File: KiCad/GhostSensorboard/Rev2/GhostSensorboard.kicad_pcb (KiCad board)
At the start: 2 copper layers, 50 x 50 mm, 43 parts, among them P1 StartModule, P2 SteeringServo, P3 Motor, P4 CONN_02X30, Q1 BSS138, Q2 BSS138, SW1 SW_Push, U1 TCA9548ARGER, U10 GP2Y0E02B, U11 GP2Y0E02B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

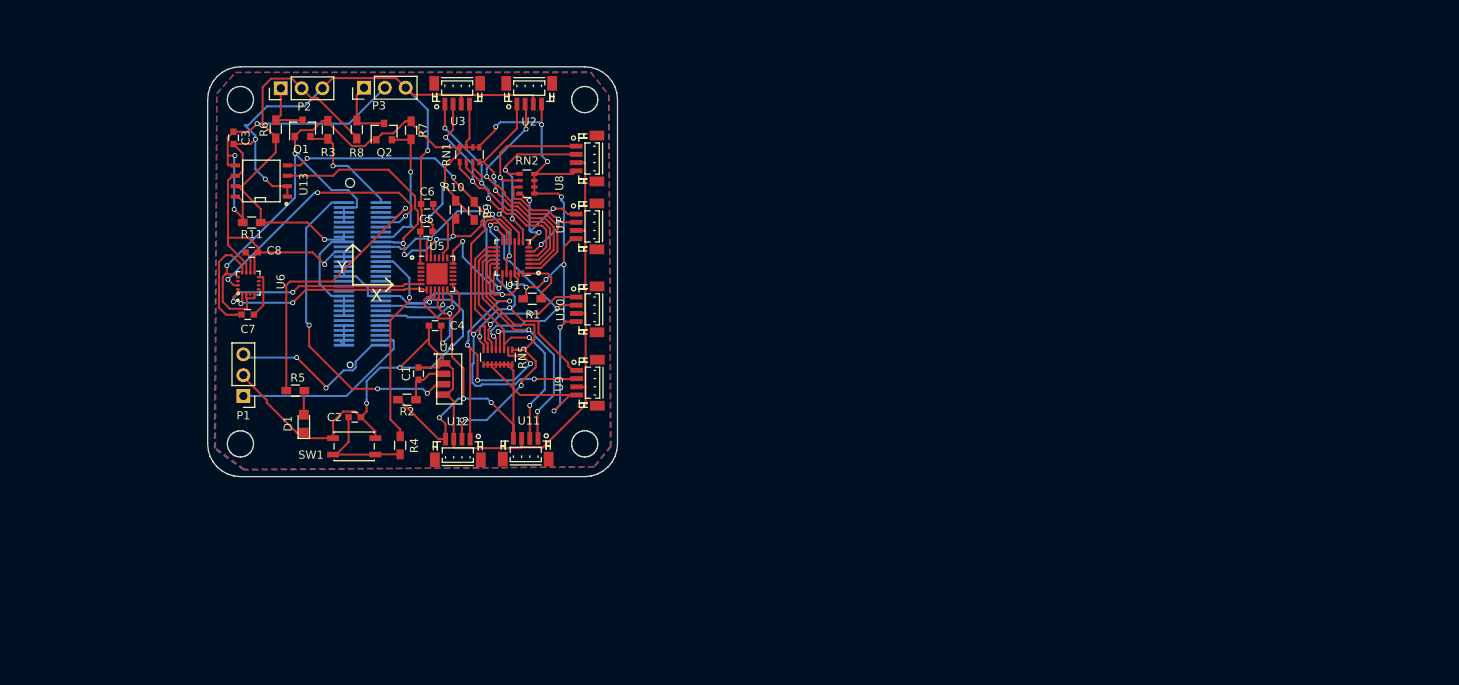
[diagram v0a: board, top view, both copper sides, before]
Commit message: Made a connectorboard
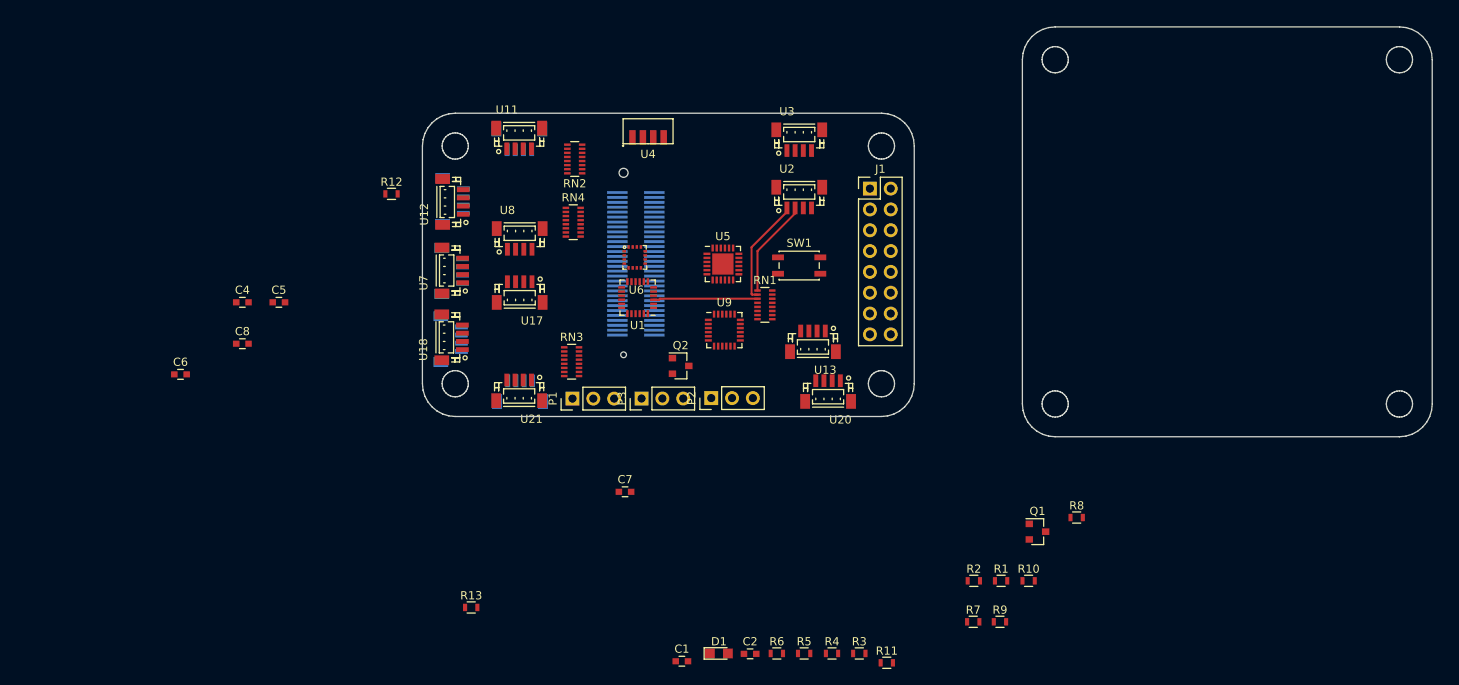
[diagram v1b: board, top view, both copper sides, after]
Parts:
- removed C3: 0.1-1uF, Capacitors_SMD:C_0603
- removed RN5: R_Pack08, Resistors_SMD:R_Array_Convex_8x0602
- added J1: CONN_02X08, Pin_Headers:Pin_Header_Straight_2x08_Pitch2.54mm, F.Cu at (171.5, 90.0)
- added R12: 2k2, Resistors_SMD:R_0603, F.Cu at (113.2, 90.6)
- added R13: 2k2, Resistors_SMD:R_0603, F.Cu at (122.9, 141.1)
- added RN3: R_Pack08, Resistors_SMD:R_Array_Convex_8x0602, F.Cu at (135.1, 111.1)
- added RN4: R_Pack08, Resistors_SMD:R_Array_Convex_8x0602, F.Cu at (135.3, 94.1)
- added U14: GP2Y0E02B, Connectors_JST:JST_SH_BM04B-SRSS-TB_04x1.00mm_Straight, B.Cu at (120.4, 108.4)
- added U15: GP2Y0E02B, Connectors_JST:JST_SH_BM04B-SRSS-TB_04x1.00mm_Straight, B.Cu at (120.6, 100.1)
- added U16: GP2Y0E02B, Connectors_JST:JST_SH_BM04B-SRSS-TB_04x1.00mm_Straight, B.Cu at (128.9, 114.7)
- added U17: GP2Y0E02B, Connectors_JST:JST_SH_BM04B-SRSS-TB_04x1.00mm_Straight, F.Cu at (128.8, 102.6)
- added U18: GP2Y0E02B, Connectors_JST:JST_SH_BM04B-SRSS-TB_04x1.00mm_Straight, F.Cu at (120.6, 108.2)
- added U19: GP2Y0E02B, Connectors_JST:JST_SH_BM04B-SRSS-TB_04x1.00mm_Straight, B.Cu at (120.7, 91.5)
- added U20: GP2Y0E02B, Connectors_JST:JST_SH_BM04B-SRSS-TB_04x1.00mm_Straight, F.Cu at (166.4, 114.7)
- added U21: GP2Y0E02B, Connectors_JST:JST_SH_BM04B-SRSS-TB_04x1.00mm_Straight, F.Cu at (128.7, 114.6)
- R1, R10, R2, R3, R4, R5, R6, R7, R8, R9: footprint Resistors_SMD:R_0603_HandSoldering -> Resistors_SMD:R_0603
- R11: value 0.1 ohm -> 2k2; footprint Resistors_SMD:R_0603_HandSoldering -> Resistors_SMD:R_0603
- RN1, RN2: value R_Pack04 -> R_Pack08; footprint Resistors_SMD:R_Array_Convex_4x0603 -> Resistors_SMD:R_Array_Convex_8x0602
- U10: moved to B.Cu
- U13: value INA219 -> GP2Y0E02B; footprint SMD_Packages:SOIC-8-N -> Connectors_JST:JST_SH_BM04B-SRSS-TB_04x1.00mm_Straight
- U9: value GP2Y0E02B -> TCA9548ARGER; footprint Connectors_JST:JST_SH_BM04B-SRSS-TB_04x1.00mm_Straight -> Housings_DFN_QFN:QFN-24_4x4mm_Pitch0.5mm
- moved Q1 102.3 mm to (192.0, 131.9), turned to 0 degrees
- moved R8 99.8 mm to (196.8, 130.1), turned to 0 degrees
- moved R11 94.3 mm to (173.6, 147.9), turned to 0 degrees
- moved R7 91.1 mm to (184.1, 142.9), turned to 0 degrees
- moved R3 91.0 mm to (170.2, 146.7), turned to 0 degrees
- moved R6 88.5 mm to (160.2, 146.7), turned to 0 degrees
- moved R10 83.3 mm to (190.9, 137.9), turned to 0 degrees
- moved R9 81.4 mm to (187.4, 142.9), turned to 0 degrees
- moved R2 72.6 mm to (184.2, 137.9), turned to 0 degrees
- moved U13 70.1 mm to (164.6, 108.6), turned to 180 degrees
- moved R5 69.9 mm to (163.5, 146.7), turned to 0 degrees
- moved R1 66.8 mm to (187.5, 137.9)
- moved P2 64.7 mm to (152.2, 115.6)
- moved SW1 58.6 mm to (162.9, 99.4), turned to 0 degrees
- moved R4 58.5 mm to (166.9, 146.7), turned to 0 degrees
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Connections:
- P4 pad 51: GPIO_SCL -> GPIO_SCL_0
- P4 pad 52: GPIO_SDA -> GPIO_SDA_0
- R1 pad 2: Net-(R1-Pad2) -> GPIO_SCL_0
- R10 pad 2: GPIO_SDA -> GPIO_SDA_1
- R11 pad 1: +5V -> +3V3
- R11 pad 2: +BATT -> GPIO_SDA_0
- R9 pad 2: GPIO_SCL -> GPIO_SCL_1
- RN1 pad 1: SD1 -> SD0
- RN1 pad 2: SC1 -> SC0
- RN1 pad 3: SD0 -> SD1
- RN1 pad 4: SC0 -> SC1
- RN1 pad 5: +3V3 -> SD2
- RN1 pad 6: +3V3 -> SC2
- RN1 pad 7: +3V3 -> SD3
- RN1 pad 8: +3V3 -> SC3
- RN2 pad 1: SD3 -> SD4
- RN2 pad 2: SC3 -> SC4
- RN2 pad 3: SD2 -> SD5
- RN2 pad 4: SC2 -> SC5
- RN2 pad 5: +3V3 -> SD6
- RN2 pad 6: +3V3 -> SC6
- RN2 pad 7: +3V3 -> SD7
- RN2 pad 8: +3V3 -> SC7
- U1 pad 19: GPIO_SCL -> GPIO_SCL_0
- U1 pad 20: GPIO_SDA -> GPIO_SDA_0
- U1 pad 24: Net-(R1-Pad2) -> Net-(R12-Pad2)
- U10 pad 1: SC5 -> SC4
- U10 pad 2: SD5 -> SD4
- U11 pad 1: SC6 -> SC5
- U11 pad 2: SD6 -> SD5
- U12 pad 1: SC7 -> SC6
- U12 pad 2: SD7 -> SD6
- U13 pad 1: GND -> SC7
- U13 pad 2: GND -> SD7
- U13 pad 3: GPIO_SDA -> GND
- U13 pad 4: GPIO_SCL -> +3V3
- U5 pad 23: GPIO_SDA -> GPIO_SDA_0
- U5 pad 24: GPIO_SCL -> GPIO_SCL_0
- U5 pad 6: MPU_SDA -> Net-(U5-Pad6)
- U5 pad 7: MPU_SCL -> Net-(U5-Pad7)
- U6 pad 1: MPU_SCL -> GPIO_SDA_0
- U6 pad 16: MPU_SDA -> GPIO_SCL_0
- U9 pad 1: SC4 -> Net-(U9-Pad1)
- U9 pad 2: SD4 -> Net-(U9-Pad2)
- U9 pad 3: GND -> Net-(U9-Pad3)
- U9 pad 4: +3V3 -> Net-(U9-Pad4)
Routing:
- net GND: track 304.2 -> 0.00 mm, vias 9 -> 0
- net +3V3: track 247.5 -> 0.00 mm, vias 17 -> 0
- net +5V: track 61.8 -> 0.00 mm, vias 1 -> 0
- net GPIO_SCL: track 57.4 -> 0.00 mm, vias 5 -> 0
- net GPIO_SDA: track 54.5 -> 0.00 mm, vias 6 -> 0
- net SD4: track 43.7 -> 0.00 mm, vias 2 -> 0
- net SC7: track 43.0 -> 0.00 mm, vias 4 -> 0
- net GPIO_IR: track 39.6 -> 0.00 mm, vias 3 -> 0
- net +BATT: track 39.2 -> 0.00 mm, vias 3 -> 0
- net SD7: track 35.9 -> 0.00 mm, vias 2 -> 0
- net SC4: track 35.7 -> 0.00 mm, vias 3 -> 0
- net SC6: track 35.2 -> 0.00 mm, vias 3 -> 0
- net GPIO_LED: track 34.8 -> 0.00 mm, vias 1 -> 0
- net GPIO_DRDY: track 33.9 -> 0.00 mm, vias 3 -> 0
- net SD6: track 32.1 -> 0.00 mm, vias 2 -> 0
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- removed copper zone on B.Cu, net GND
- removed copper zone on F.Cu, net GND
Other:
- board size 50 x 50 mm -> 123.2 x 50 mm
- net class Default: via_dia 0.6 -> 0.8
- rule pad_to_mask_clearance: 0.2 -> 0
- board text removed: "Frode Lillerud 27.feb 2017"
- board text removed: "X"
- board text removed: "Y"

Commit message: Working on the Encoder
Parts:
- removed C4: 0.1uF, Capacitors_SMD:C_0603
- removed C5: 10nF, Capacitors_SMD:C_0603
- removed C6: 2.2nF, Capacitors_SMD:C_0603
- removed C7: 0.22uF, Capacitors_SMD:C_0603
- removed C8: 4.7uF, Capacitors_SMD:C_0603
- removed U5: MPU-6050, Housings_DFN_QFN:QFN-24-1EP_4x4mm_Pitch0.5mm
- removed U6: HMC5883, NorBotKiCadFootprints:HMC5883
- J1: value CONN_02X08 -> CONN_02X05; footprint Pin_Headers:Pin_Header_Straight_2x08_Pitch2.54mm -> Pin_Headers:Pin_Header_Straight_2x05_Pitch2.54mm
- U10, U15, U16: moved to F.Cu
- moved U12 116.0 mm to (236.7, 89.5), turned to 270 degrees
- moved U21 109.2 mm to (236.7, 98.1), turned to 270 degrees
- moved U16 108.3 mm to (236.9, 106.5), turned to 270 degrees
- moved U11 107.9 mm to (236.6, 81.1), turned to 270 degrees
- moved U17 101.7 mm to (229.5, 116.8)
- moved R12 99.5 mm to (205.6, 127.4)
- moved U8 94.7 mm to (221.2, 116.9), turned to 180 degrees
- moved U7 94.1 mm to (213.1, 117.0), turned to 180 degrees
- moved RN4 93.9 mm to (228.4, 81.6)
- moved U18 84.7 mm to (204.7, 117.1), turned to 180 degrees
- moved RN3 76.3 mm to (211.4, 110.8), turned to 90 degrees
- moved U1 75.0 mm to (218.1, 99.4)
- moved U20 73.8 mm to (227.7, 73.5), turned to 0 degrees
- moved U19 73.7 mm to (193.7, 82.1)
- moved U15 73.6 mm to (193.7, 107.7), turned to 90 degrees
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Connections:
- J1 pad 10: GPIO_21 -> GND
- J1 pad 2: GND -> +5V
- J1 pad 3: +3V3 -> (no net)
- J1 pad 4: GND -> (no net)
- J1 pad 5: GPIO_4 -> (no net)
- J1 pad 6: GPIO_32 -> (no net)
- J1 pad 7: GPIO_16 -> (no net)
- J1 pad 8: GPIO_33 -> (no net)
- J1 pad 9: GPIO_17 -> (no net)
- P3 pad 2: +BATT -> +5V
- P4 pad 10: Net-(P4-Pad10) -> (no net)
- P4 pad 17: Net-(P4-Pad17) -> (no net)
- P4 pad 18: Net-(P4-Pad18) -> (no net)
- P4 pad 19: Net-(P4-Pad19) -> (no net)
- P4 pad 25: Net-(P4-Pad25) -> (no net)
- P4 pad 33: Net-(P4-Pad33) -> (no net)
- P4 pad 34: Net-(P4-Pad34) -> (no net)
- P4 pad 35: Net-(P4-Pad35) -> (no net)
- P4 pad 36: Net-(P4-Pad36) -> (no net)
- P4 pad 37: GPIO_INT -> (no net)
- P4 pad 38: Net-(P4-Pad38) -> (no net)
- P4 pad 39: GPIO_FSYNC -> (no net)
- P4 pad 40: Net-(P4-Pad40) -> (no net)
- P4 pad 42: Net-(P4-Pad42) -> (no net)
- P4 pad 43: Net-(P4-Pad43) -> (no net)
- P4 pad 44: Net-(P4-Pad44) -> (no net)
- P4 pad 45: Net-(P4-Pad45) -> (no net)
- P4 pad 46: Net-(P4-Pad46) -> (no net)
- P4 pad 47: Net-(P4-Pad47) -> (no net)
- P4 pad 49: Net-(P4-Pad49) -> (no net)
- P4 pad 50: Net-(P4-Pad50) -> (no net)
- P4 pad 54: Net-(P4-Pad54) -> (no net)
- P4 pad 55: Net-(P4-Pad55) -> (no net)
- P4 pad 56: GPIO_DRDY -> (no net)
- P4 pad 58: Net-(P4-Pad58) -> (no net)
- P4 pad 59: Net-(P4-Pad59) -> (no net)
- P4 pad 6: Net-(P4-Pad6) -> (no net)
- U9 pad 1: Net-(U9-Pad1) -> (no net)
- U9 pad 10: Net-(U9-Pad10) -> (no net)
- U9 pad 11: Net-(U9-Pad11) -> (no net)
- U9 pad 12: Net-(U9-Pad12) -> (no net)
- U9 pad 13: Net-(U9-Pad13) -> (no net)
- U9 pad 14: Net-(U9-Pad14) -> (no net)
- U9 pad 15: Net-(U9-Pad15) -> (no net)
- U9 pad 16: Net-(U9-Pad16) -> (no net)
- U9 pad 17: Net-(U9-Pad17) -> (no net)
- U9 pad 2: Net-(U9-Pad2) -> (no net)
- U9 pad 3: Net-(U9-Pad3) -> (no net)
- U9 pad 4: Net-(U9-Pad4) -> (no net)
- U9 pad 5: Net-(U9-Pad5) -> (no net)
- U9 pad 6: Net-(U9-Pad6) -> (no net)
- U9 pad 7: Net-(U9-Pad7) -> (no net)
- U9 pad 8: Net-(U9-Pad8) -> (no net)
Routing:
- net SC0: track 13.0 -> 0.00 mm
- net SD1: track 12.7 -> 0.00 mm
- net SD0: track 12.0 -> 0.00 mm
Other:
- board size 123.2 x 50 mm -> 171.2 x 50 mm

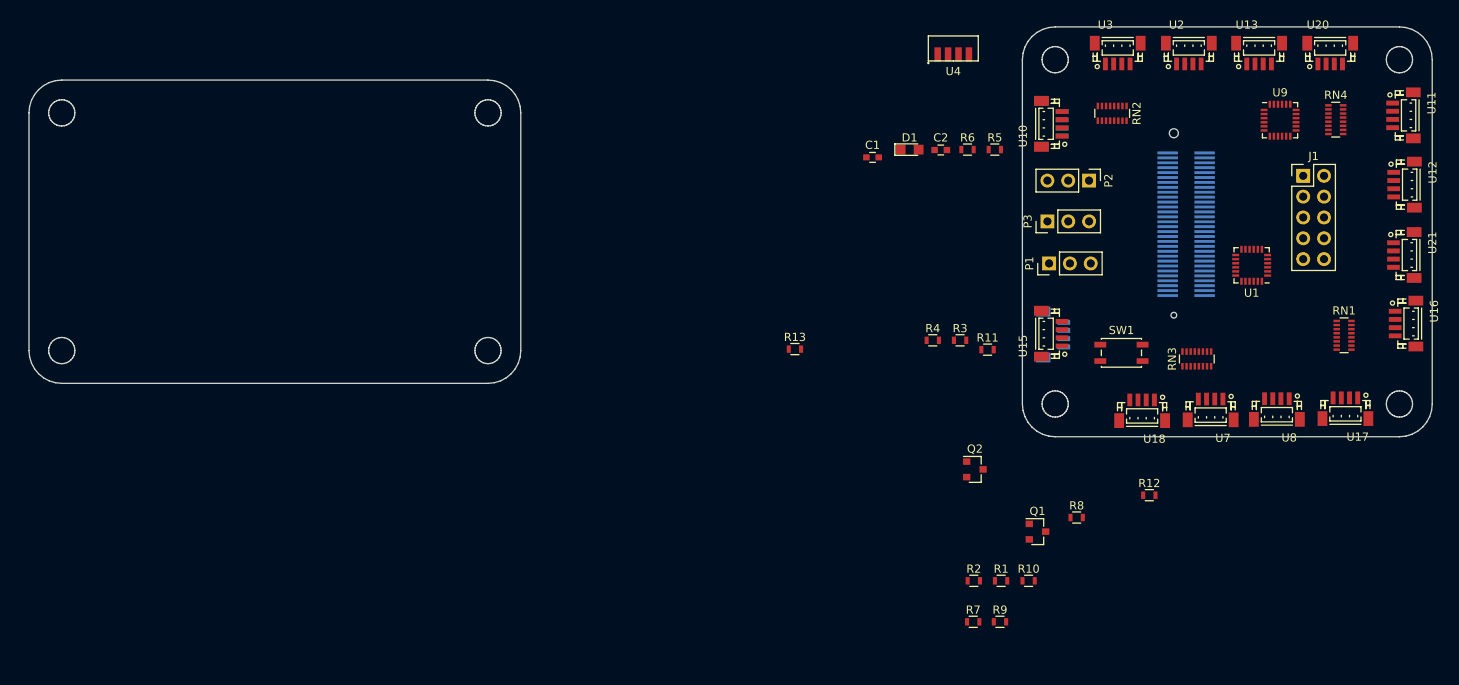
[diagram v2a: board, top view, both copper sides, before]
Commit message: Ready to start routing. Schematics should be done.
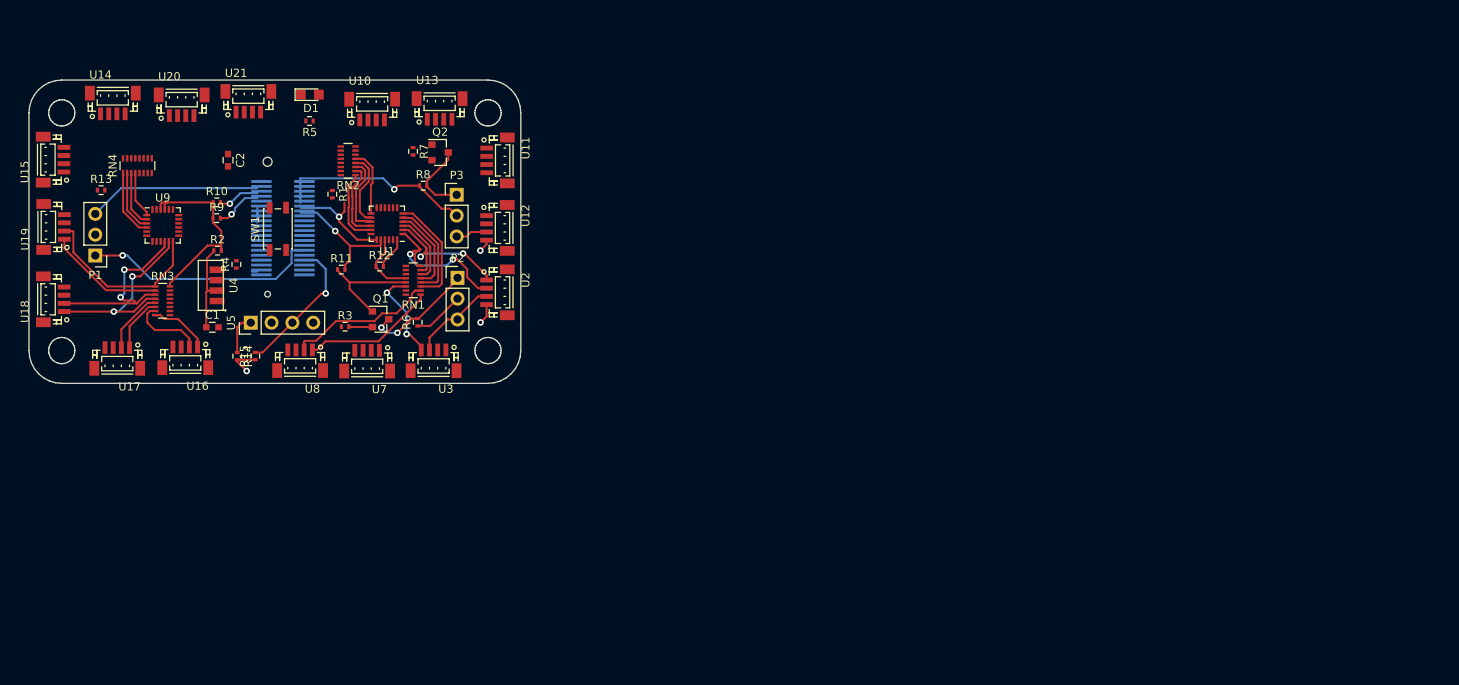
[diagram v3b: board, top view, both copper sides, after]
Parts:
- removed J1: CONN_02X05, Pin_Headers:Pin_Header_Straight_2x05_Pitch2.54mm
- removed P4: CONN_02X30, hrs-fx8c:hrs-fx8c-60s-sv
- added J2: CONN_02X20, hrs-fx8c:hrs-fx8c-40s-sv5, B.Cu at (99.6, 94.8)
- added R14: 270, Resistors_SMD:R_0402, F.Cu at (94.3, 110.5)
- added R15: 10k, Resistors_SMD:R_0402, F.Cu at (96.6, 110.4)
- added U5: Transmissive_Photo_Interrupter, Pin_Headers:Pin_Header_Straight_1x04_Pitch2.54mm, F.Cu at (96.0, 106.4)
- R1, R10, R11, R12, R13, R2, R3, R4, R5, R6, R7, R8, R9: footprint Resistors_SMD:R_0603 -> Resistors_SMD:R_0402
- U14, U19: moved to F.Cu
- moved U17 150.0 mm to (79.7, 110.7)
- moved U16 148.9 mm to (88.0, 110.6), turned to 180 degrees
- moved RN4 146.3 mm to (82.2, 87.2), turned to 90 degrees
- moved U21 142.2 mm to (95.7, 79.4), turned to 0 degrees
- moved U20 140.3 mm to (87.6, 79.8)
- moved U9 136.9 mm to (85.3, 94.5)
- moved U18 133.5 mm to (72.0, 103.5), turned to 90 degrees
- moved RN3 126.4 mm to (85.2, 103.7), turned to 0 degrees
- moved U15 123.6 mm to (71.9, 86.5)
- moved U19 122.4 mm to (72.0, 94.7), turned to 90 degrees
- moved U8 119.3 mm to (102.0, 110.9)
- moved U14 118.2 mm to (79.2, 79.6), turned to 0 degrees
- moved P1 116.4 mm to (77.0, 98.2), turned to 180 degrees
- moved RN1 113.8 mm to (115.8, 101.2), turned to 180 degrees
- moved U12 110.8 mm to (126.0, 94.8)
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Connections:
- net GPIO_MOTOR renamed IO27
- net GPIO_SCL_0 renamed IO14
- net GPIO_SCL_1 renamed IO32
- net GPIO_SDA_0 renamed IO13
- net GPIO_SDA_1 renamed IO33
- net GPIO_STEERING renamed IO26
- net MotorPWM renamed MOTOR_5V_PWM
- net SteeringPWM renamed STEERING_5V_PWM
- D1 pad 1: GND -> LED
- P1 pad 1: GPIO_StartModule_VCC -> IO17
- P1 pad 3: GPIO_StartModule -> IO25
- R4 pad 2: GPIO_BUTTON -> BUTTON
- R5 pad 2: GPIO_LED -> +3V3
- RN1 pad 1: SD0 -> SC3
- RN1 pad 2: SC0 -> SD3
- RN1 pad 3: SD1 -> SC2
- RN1 pad 4: SC1 -> SD2
- RN1 pad 5: SD2 -> SC1
- RN1 pad 6: SC2 -> SD1
- RN1 pad 7: SD3 -> SC0
- RN1 pad 8: SC3 -> SD0
- RN2 pad 1: SD4 -> SC7
- RN2 pad 2: SC4 -> SD7
- RN2 pad 3: SD5 -> SC6
- RN2 pad 4: SC5 -> SD6
- RN2 pad 5: SD6 -> SC5
- RN2 pad 6: SC6 -> SD5
- RN2 pad 7: SD7 -> SC4
- RN2 pad 8: SC7 -> SD4
- RN3 pad 1: SD8 -> SD13
- RN3 pad 2: SC8 -> SC13
- RN3 pad 3: SD9 -> SD12
- RN3 pad 4: SC9 -> SC12
- RN3 pad 5: SD10 -> SD11
- RN3 pad 6: SC10 -> SC11
- RN3 pad 7: SD11 -> SD10
- RN3 pad 8: SC11 -> SC10
- RN4 pad 1: SD12 -> SC9
- RN4 pad 2: SC12 -> SD9
- RN4 pad 3: SD13 -> SC8
- RN4 pad 4: SC13 -> SD8
- RN4 pad 5: SD14 -> SC15
- RN4 pad 6: SC14 -> SD15
- RN4 pad 7: SD15 -> SC14
- RN4 pad 8: SC15 -> SD14
- U4 pad 3: GPIO_IR -> IO22
- U9 pad 1: (no net) -> SD8
- U9 pad 10: (no net) -> SD12
- U9 pad 11: (no net) -> SC12
- U9 pad 12: (no net) -> SD13
- U9 pad 13: (no net) -> SC13
- U9 pad 14: (no net) -> SD14
- U9 pad 15: (no net) -> SC14
- U9 pad 16: (no net) -> SD15
- U9 pad 17: (no net) -> SC15
- U9 pad 2: (no net) -> SC8
- U9 pad 3: (no net) -> SD9
- U9 pad 4: (no net) -> SC9
- U9 pad 5: (no net) -> SD10
- U9 pad 6: (no net) -> SC10
- U9 pad 7: (no net) -> SD11
- U9 pad 8: (no net) -> SC11
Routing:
- net +5V: track 0.00 -> 79.1 mm, vias 0 -> 2
- net +3V3: track 0.00 -> 60.5 mm, vias 0 -> 4
- net IO17: track 0.00 -> 29.0 mm, vias 0 -> 1
- net SD12: track 0.00 -> 24.2 mm, vias 0 -> 2
- net SC12: track 0.00 -> 24.0 mm, vias 0 -> 2
- net SD13: track 0.00 -> 21.8 mm
- net IO25: track 0.00 -> 21.1 mm
- net SD0: track 0.00 -> 19.8 mm, vias 0 -> 2
- net SC0: track 0.00 -> 18.4 mm, vias 0 -> 2
- net SD3: track 0.00 -> 18.1 mm
- net ENCODER: track 0.00 -> 17.6 mm, vias 0 -> 1
- net SC3: track 0.00 -> 16.3 mm
- net IO13: track 0.00 -> 15.3 mm, vias 0 -> 1
- net GND: track 0.00 -> 14.6 mm
- net SC13: track 0.00 -> 14.3 mm
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- added copper zone on 3v3_PLANE, net +3V3
- added copper zone on GND_PLANE, net GND
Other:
- board size 171.2 x 50 mm -> 60 x 37 mm
- copper layers 2 -> 4
